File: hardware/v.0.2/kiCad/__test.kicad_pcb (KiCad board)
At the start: 2 copper layers, 40.8 x 14.7 mm, 29 parts, among them IC1 ATSHA204A, P1 USB_A, P2 1, P3 3, P4 2, SW1 SW_PUSH, SW2 SW_PUSH, SW3 SW_PUSH, SW4 SW_PUSH, SW5 SW_PUSH, U1 STM32F103C8, U2 TLV70033DDC, Y1 Crystal

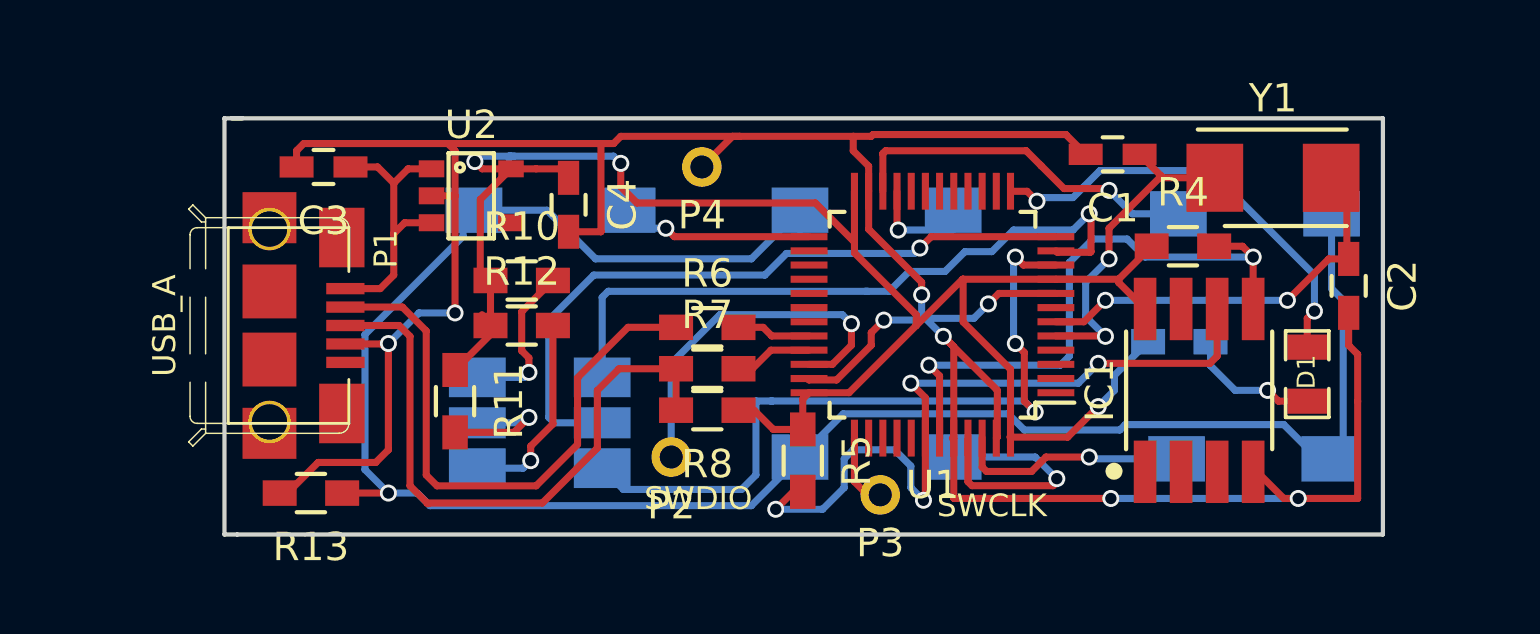
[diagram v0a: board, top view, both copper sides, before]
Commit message: Убрал баг с платы
На второй плате обнаружился баг, забыл развести конденсатор на reset и
замкнуть ноги 4-5 usb-разъема. Заодно сделал универсальным посадочное
место SO8, теперь туда можно припаять как ATHSA204A, так и 24cXX eeprom.
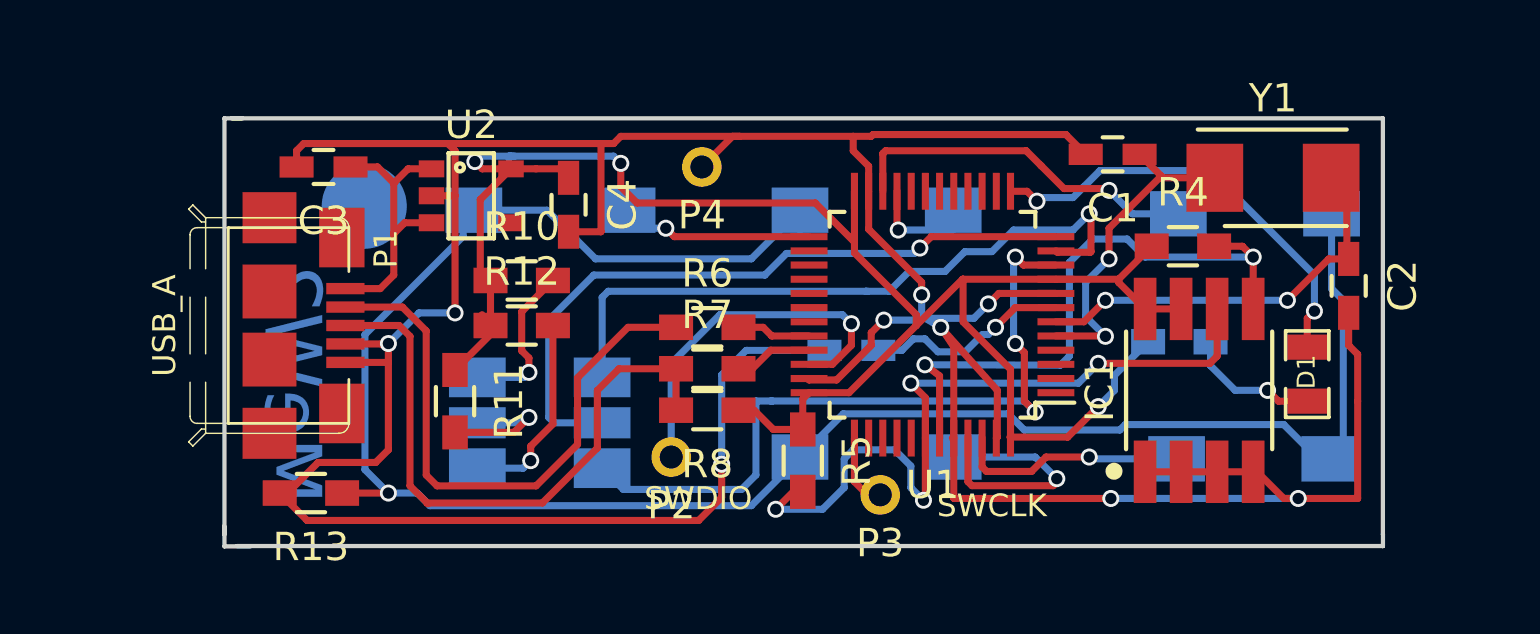
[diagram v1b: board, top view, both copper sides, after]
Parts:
- added C5: 0.1mf, Capacitors_SMD:C_0603_HandSoldering, B.Cu at (53.1, 36.9)
- added REF**: Measurement_Point_Round-SMD-Pad_Big, Measurement_Points:Measurement_Point_Round-SMD-Pad_Big, B.Cu at (35.9, 31.8)
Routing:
- net GND: track 107.1 -> 137.4 mm, vias 8 -> 9
- net Net-(C5-Pad1): track 0.00 -> 7.26 mm, vias 0 -> 1
- net +3V3: track 65.6 -> 66.9 mm
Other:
- board size 40.8 x 14.7 mm -> 40.8 x 15.1 mm
- board text added: "MeW2"

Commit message: Мелкая правка платы
Поставил чуть другие кнопки, тех не найти.
Поставил реперы.
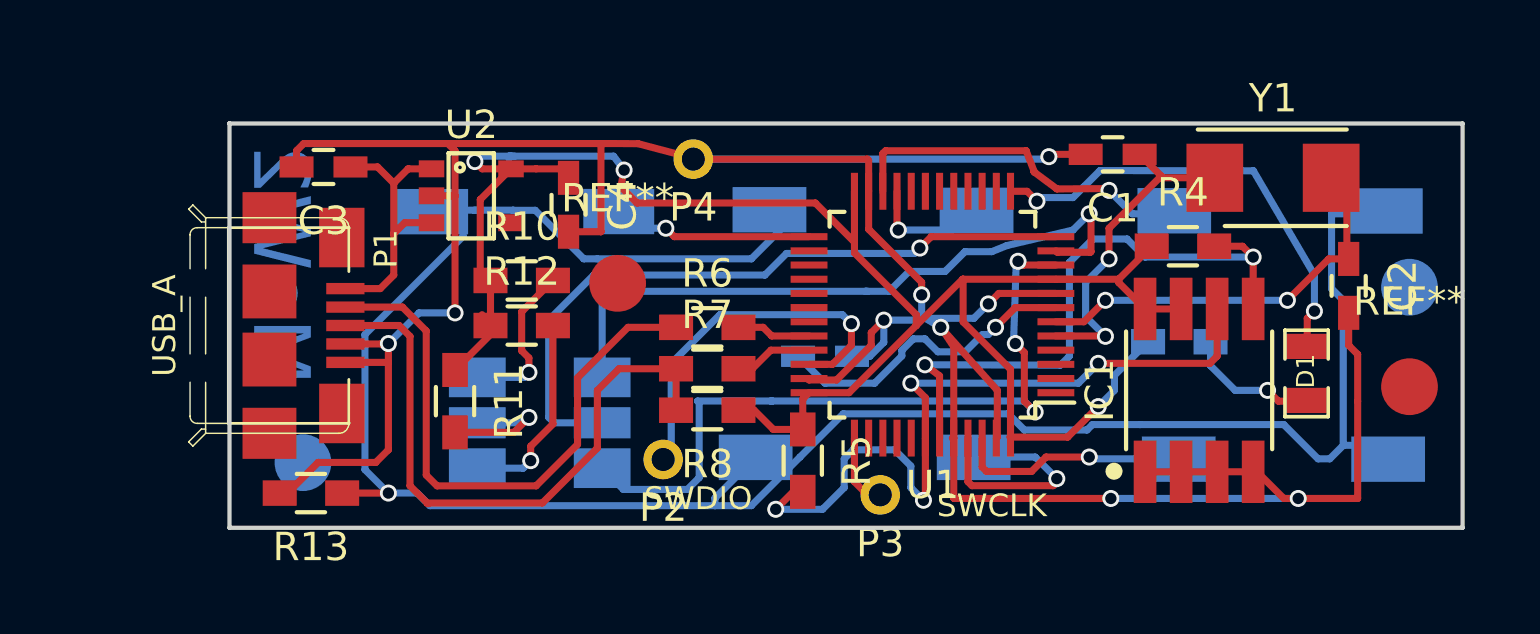
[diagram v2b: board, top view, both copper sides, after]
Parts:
- added REF**: Measurement_Point_Round-SMD-Pad_Big, Measurement_Points:Measurement_Point_Round-SMD-Pad_Big, F.Cu at (72.8, 38.2)
- added REF**: Measurement_Point_Round-SMD-Pad_Big, Measurement_Points:Measurement_Point_Round-SMD-Pad_Big, B.Cu at (33.8, 40.8)
- added REF**: Measurement_Point_Round-SMD-Pad_Big, Measurement_Points:Measurement_Point_Round-SMD-Pad_Big, F.Cu at (44.8, 34.5)
- moved REF** 37.0 mm to (72.8, 34.7)
- moved SW2 1.13 mm to (68.4, 40.7)
- moved C5 0.95 mm to (52.2, 37.1), turned to 0 degrees
- moved SW5 0.94 mm to (41.5, 32.0)
- moved SW4 0.81 mm to (68.1, 32.0)
- moved P4 0.41 mm to (47.5, 30.1)
- moved SW1 0.39 mm to (53.6, 40.7)
- moved P2 0.30 mm to (46.5, 40.7)
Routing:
- net GND: track 137.4 -> 118.0 mm
- net Net-(R13-Pad1): track 71.1 -> 78.1 mm
- net Net-(C5-Pad1): track 7.26 -> 11.1 mm
- net /LED_READY: track 15.6 -> 16.1 mm
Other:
- board size 40.8 x 15.1 mm -> 43.5 x 14.3 mm

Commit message: Мелкие правки платы
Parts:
- removed P1: USB_A, user:USB_MICRO_B_SMD
- added CON1: USB-MICRO-B, user:USB_MICRO_B_SMD, F.Cu at (30.4, 36.0)
- added REF**: USB_A, usb-male-A-smd:USB_A, B.Cu at (32.5, 36.0)
- moved REF** 0.86 mm to (34.3, 41.5)
- moved R13 0.61 mm to (34.6, 41.9)
- moved C3 0.21 mm to (34.5, 30.2)
- moved SW4 0.17 mm to (68.1, 31.8)
- moved SW3 0.12 mm to (54.0, 31.8)
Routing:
- net Net-(C3-Pad1): track 9.94 -> 24.8 mm, vias 0 -> 1
- net Net-(P1-Pad3): track 22.0 -> 33.4 mm, vias 0 -> 1
- net Net-(P1-Pad2): track 20.9 -> 30.3 mm, vias 0 -> 1
- net GND: track 118.0 -> 126.0 mm, vias 9 -> 10
- net /LED_B: track 25.8 -> 31.4 mm
- net Net-(C1-Pad1): track 11.8 -> 12.9 mm
- net /LED_R: track 23.7 -> 24.4 mm
- net /I2C_SDA_1: track 21.9 -> 22.4 mm
- net Net-(D2-Pad5): track 4.72 -> 5.24 mm
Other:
- board size 43.5 x 14.3 mm -> 45.9 x 14.2 mm
- net class Default: via_dia 0.6 -> 0.8
- board text removed: "MeW2"
